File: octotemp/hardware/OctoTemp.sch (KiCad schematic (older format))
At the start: 46 parts, among them P1 CONN_02X03, P10 CONN_01X02, P11 CONN_01X02, P12 CONN_01X02, P13 CONN_01X02, P14 CONN_01X02, P15 CONN_01X02, P16 CONN_01X02, P17 CONN_01X02, P2 CONN_01X02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

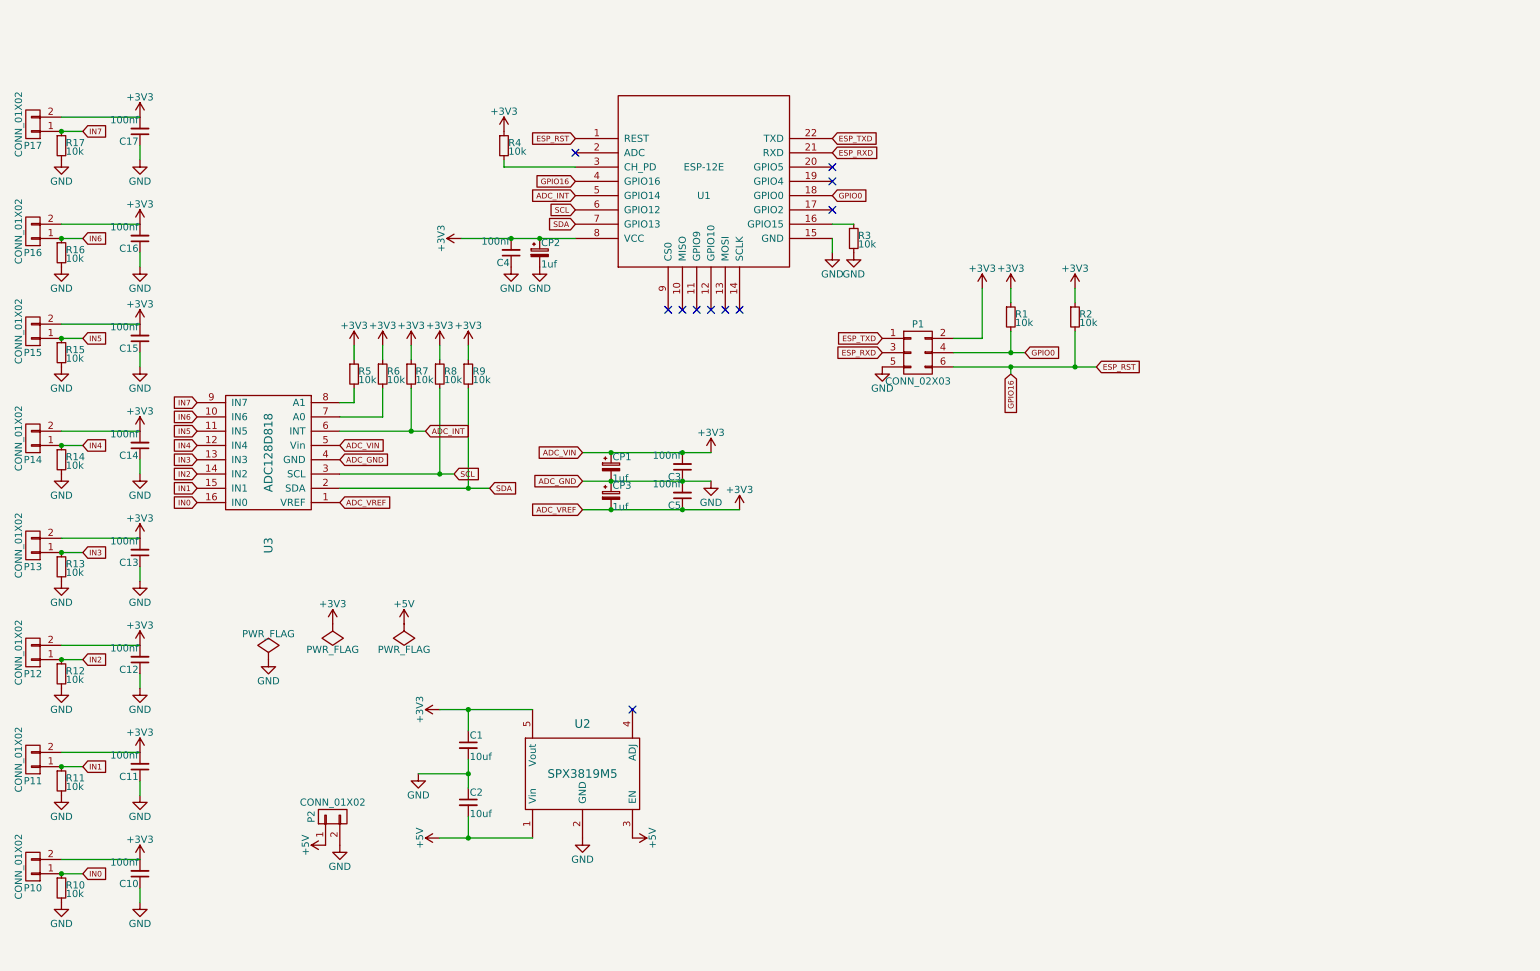
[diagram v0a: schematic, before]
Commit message: Octotemp board with 2 1x8 pin JST connectors.
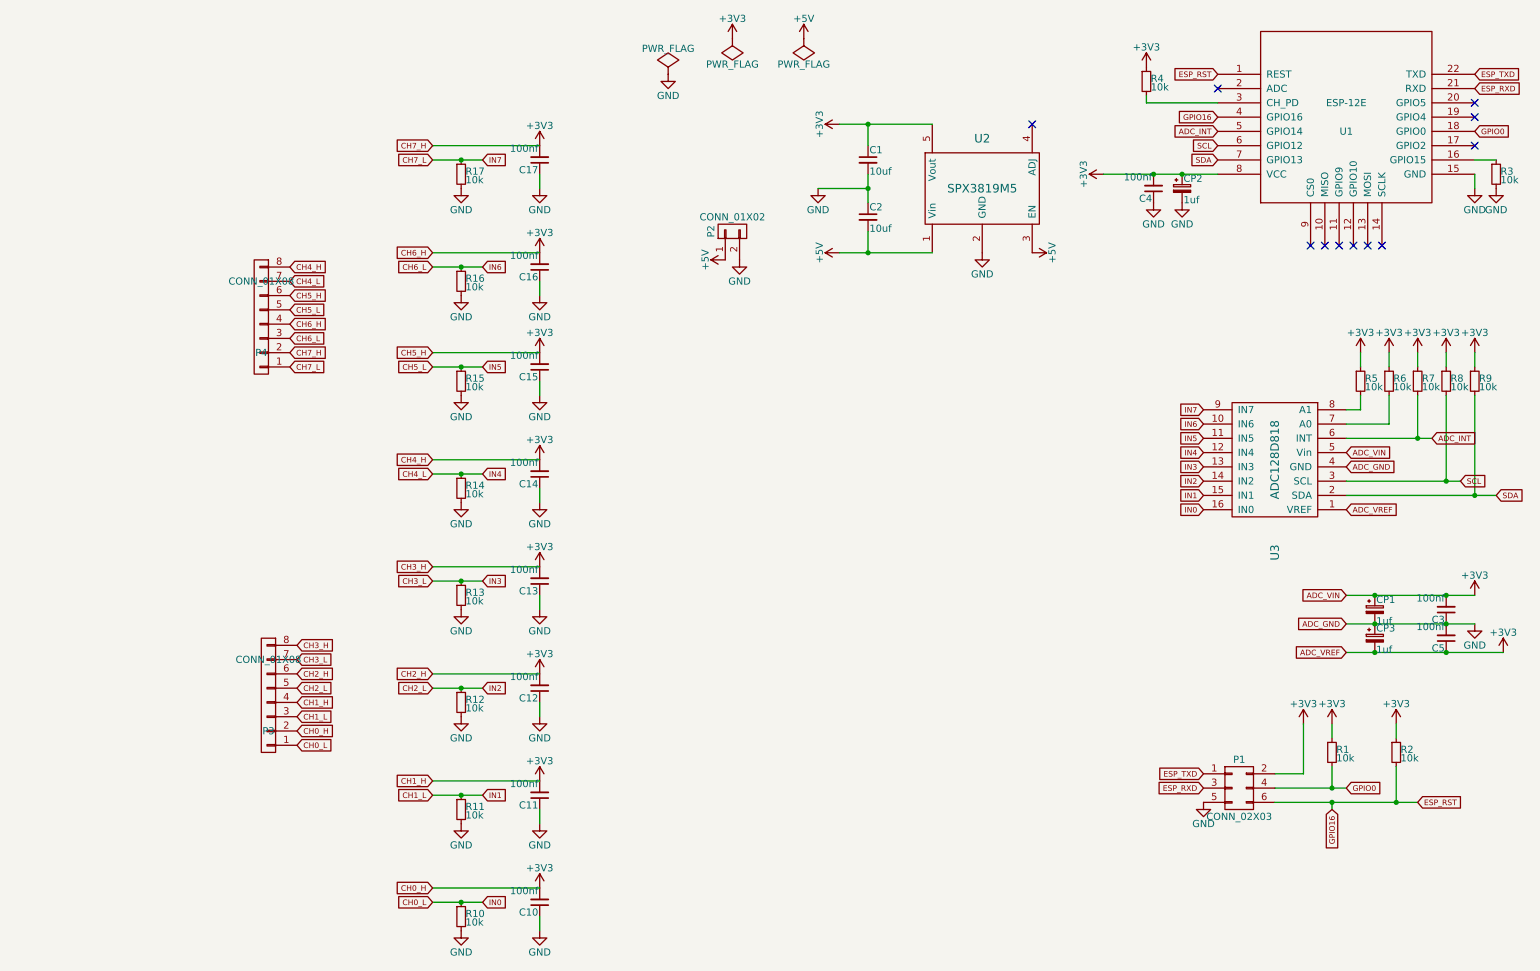
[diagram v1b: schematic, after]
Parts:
- removed P10, P11, P12, P13, P14, P15, P16, P17: CONN_01X02, w_conn_jst-ph:b2b-ph-kl, symbol CONN_01X02
- added P3, P4: CONN_01X08, Socket_Strips:Socket_Strip_Straight_2x04, symbol CONN_01X08
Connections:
- net +3V3: now also P3.2 (P2), P3.4 (P4), P3.6 (P6), P3.8 (P8), P4.2 (P2), P4.4 (P4), P4.6 (P6), P4.8 (P8)
- net IN0 renamed CH0_L
- net CH0_L: now also P3.1 (P1)
- net IN1 renamed CH1_L
- net CH1_L: now also P3.3 (P3)
- net IN2 renamed CH2_L
- net CH2_L: now also P3.5 (P5)
- net IN3 renamed CH3_L
- net CH3_L: now also P3.7 (P7)
- net IN4 renamed CH4_L
- net CH4_L: now also P4.7 (P7)
- net IN5 renamed CH5_L
- net CH5_L: now also P4.5 (P5)
- net IN6 renamed CH6_L
- net CH6_L: now also P4.3 (P3)
- net IN7 renamed CH7_L
- net CH7_L: now also P4.1 (P1)
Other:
- moved on the sheet: C1, C10, C11, C12, C13, C14, C15, C16, C17, C2, C3, C4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
